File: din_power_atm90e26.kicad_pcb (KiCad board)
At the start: 2 copper layers, 86.9 x 32.8 mm, 60 parts, among them J1 CONN_01X06, J2 VBAT, J3 CONN_01X08, J4 CONN_02X18, J5 CONN_01X08, U1 MCP73831-2-OT, U2 TLV1117-33, U3 TLV1117-33, U4 Hi-Link_SMPS, U5 dc-dc

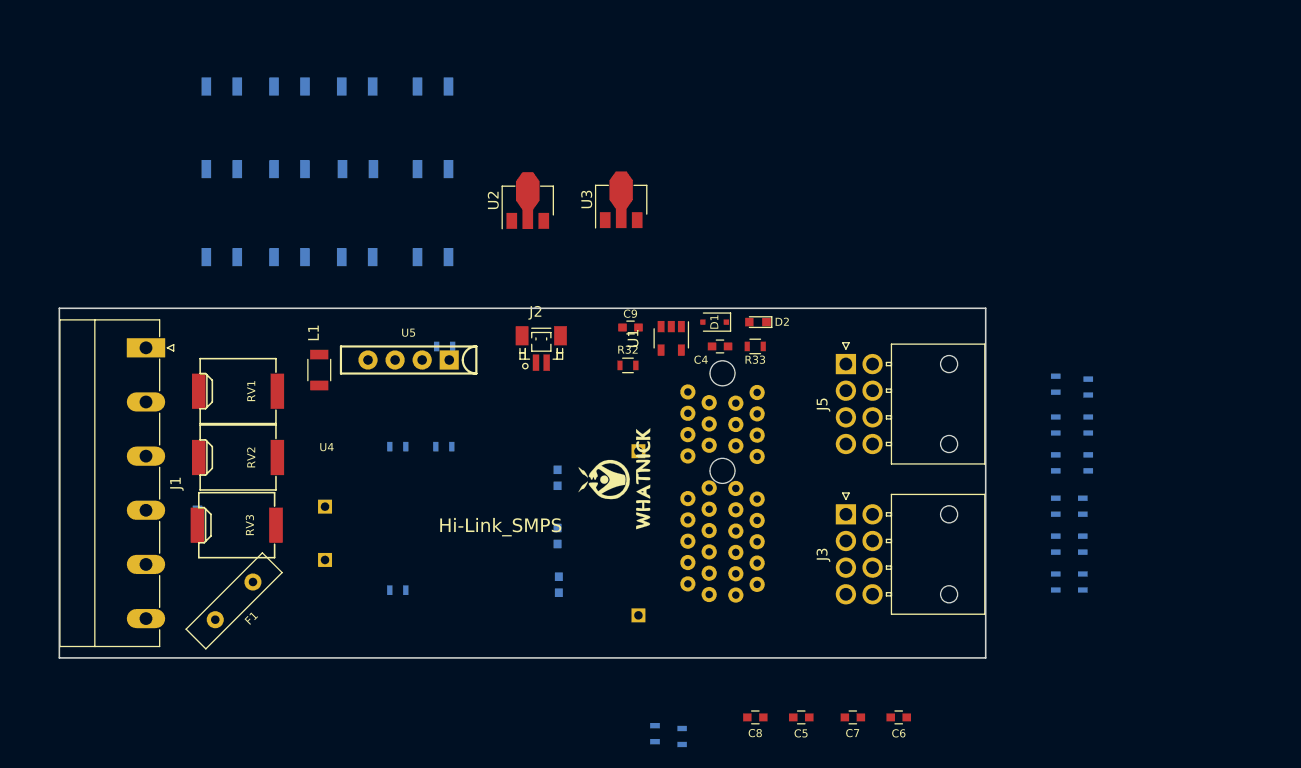
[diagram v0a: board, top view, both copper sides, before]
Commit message: Layout footprints
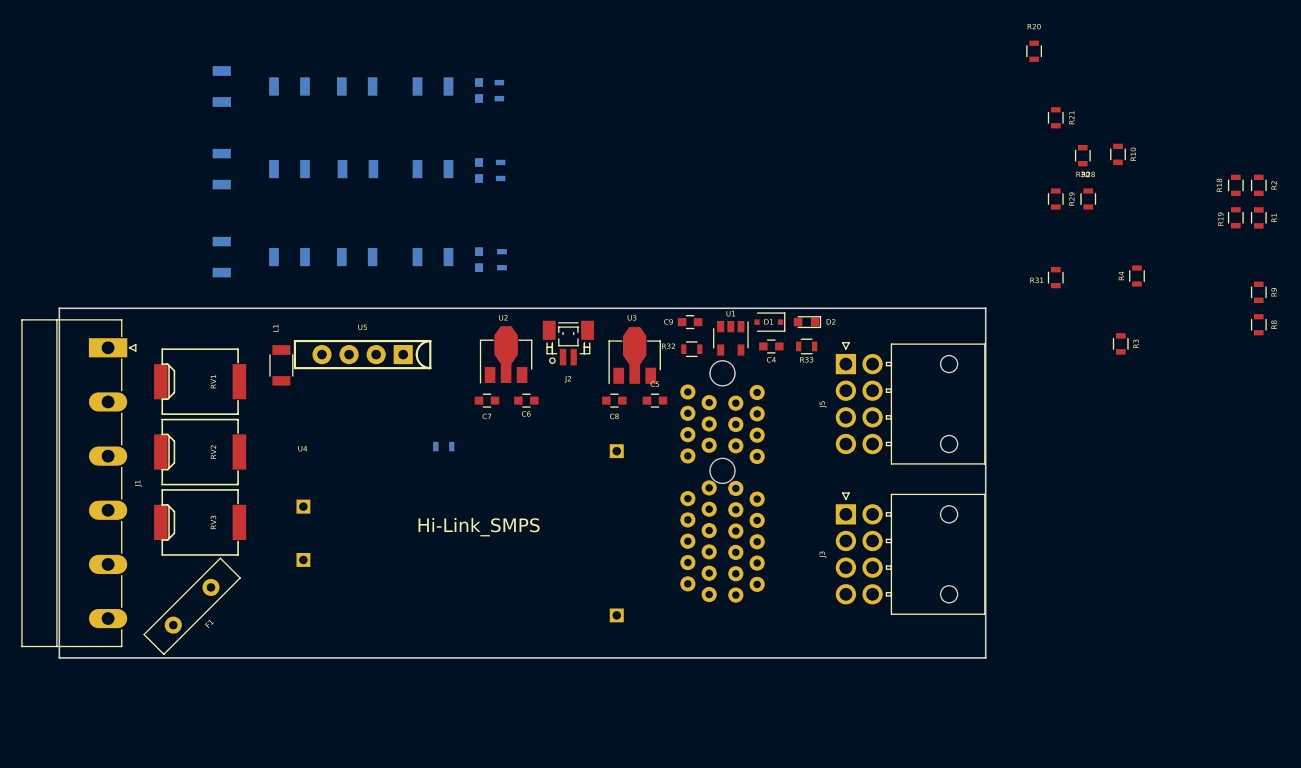
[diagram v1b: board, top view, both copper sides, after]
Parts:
- G1: moved to B.Cu
- R1, R10, R18, R19, R2, R20, R21, R28, R29, R3, R30, R31, R4, R8, R9: moved to F.Cu
- moved R3 88.1 mm to (205.5, 48.8), turned to 270 degrees
- moved R9 85.5 mm to (218.4, 44.0), turned to 270 degrees
- moved R8 81.6 mm to (218.4, 47.0), turned to 270 degrees
- moved R1 74.5 mm to (218.4, 37.0), turned to 270 degrees
- moved R10 65.7 mm to (205.2, 31.0), turned to 270 degrees
- moved R25 61.9 mm to (147.2, 25.0), turned to 90 degrees
- moved R4 60.7 mm to (207.0, 42.4), turned to 90 degrees
- moved R26 60.1 mm to (147.3, 32.5), turned to 90 degrees
- moved R27 54.2 mm to (147.4, 40.9), turned to 90 degrees
- moved R20 49.8 mm to (197.4, 21.3), turned to 90 degrees
- moved C6 45.9 mm to (149.7, 54.1), turned to 180 degrees
- moved C7 45.4 mm to (146.0, 54.1)
- moved R2 40.7 mm to (218.4, 33.9), turned to 270 degrees
- moved R21 40.0 mm to (199.4, 27.6), turned to 90 degrees
- moved C3 37.1 mm to (145.3, 25.0)
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
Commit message: Layout footprints
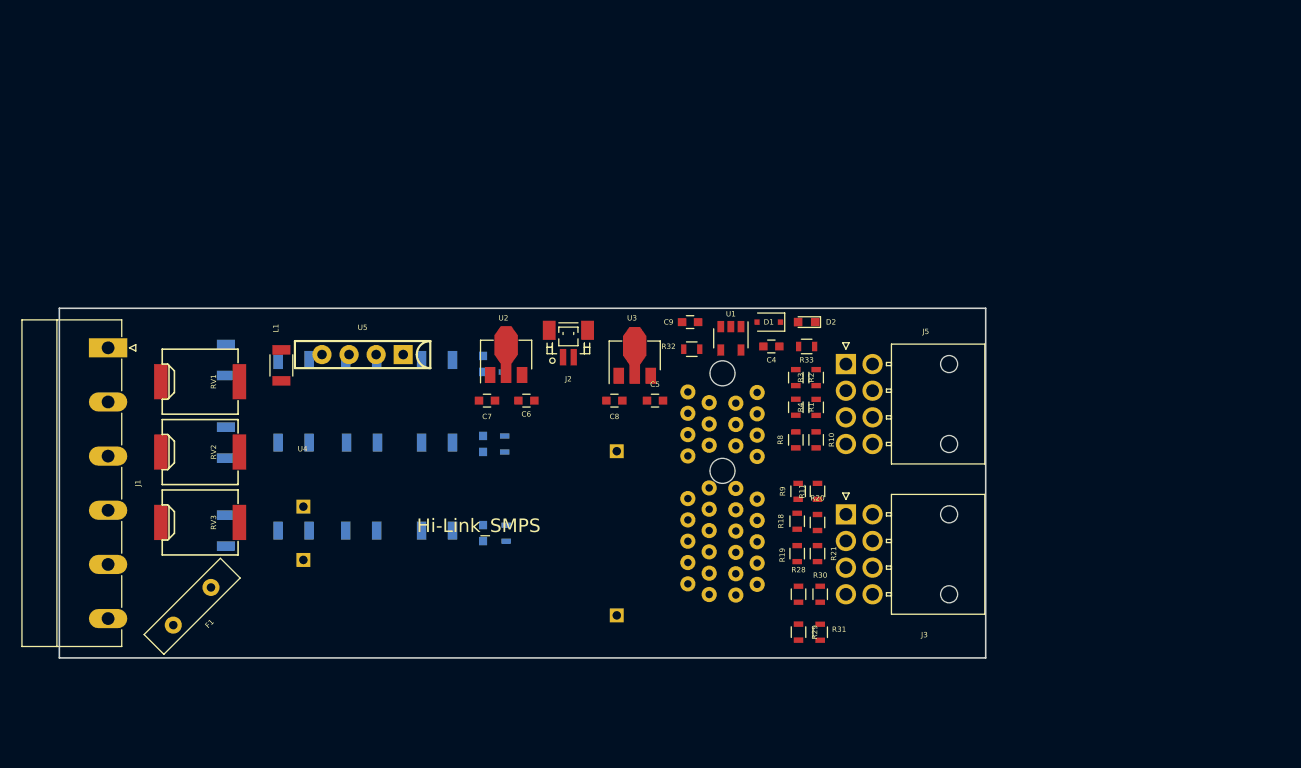
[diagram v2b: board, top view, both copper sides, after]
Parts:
- R11: moved to F.Cu
- moved R18 51.8 mm to (175.1, 65.4)
- moved R19 51.8 mm to (175.1, 68.5)
- moved R20 48.7 mm to (177.0, 65.6)
- moved R30 48.0 mm to (177.3, 72.3), turned to 90 degrees
- moved R29 47.3 mm to (175.3, 75.8)
- moved R9 47.1 mm to (175.2, 62.6), turned to 90 degrees
- moved R2 47.0 mm to (175.0, 52.0)
- moved R1 46.9 mm to (175.0, 54.8)
- moved R21 46.6 mm to (177.0, 68.5)
- moved R28 46.0 mm to (175.3, 72.3)
- moved R8 44.8 mm to (175.0, 57.8), turned to 90 degrees
- moved R31 39.9 mm to (177.3, 75.9), turned to 90 degrees
- moved R10 39.0 mm to (176.9, 57.8)
- moved R11 35.3 mm to (177.0, 62.6), turned to 90 degrees
- moved R4 32.5 mm to (176.9, 54.8)
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
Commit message: Changes from urbito
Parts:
- C1, C2, C3, R12, R13, R14, R15, R16, R17, R22, R23, R24, R25, R26, R27, R5, R6, R7: moved to F.Cu
- R10, R11, R20, R21, R3, R30, R31, R4, U4: moved to B.Cu
- moved R6 34.3 mm to (154.5, 67.6), turned to 90 degrees
- moved R13 31.2 mm to (154.5, 74.2), turned to 90 degrees
- moved F1 24.4 mm to (141.4, 59.7)
- moved R16 22.4 mm to (149.8, 74.2), turned to 270 degrees
- moved U5 21.9 mm to (152.0, 62.7)
- moved R26 17.6 mm to (142.4, 74.9), turned to 270 degrees
- moved C1 17.6 mm to (140.4, 75.0), turned to 90 degrees
- moved R23 16.6 mm to (145.2, 74.2), turned to 90 degrees
- moved U1 14.5 mm to (154.5, 49.9)
- moved C7 14.4 mm to (131.7, 53.6)
- moved D1 14.1 mm to (158.8, 49.9), turned to 90 degrees
- moved U2 13.9 mm to (133.9, 49.5)
- moved C6 13.8 mm to (135.9, 53.5)
- moved R33 13.4 mm to (162.8, 50.8)
- moved R27 12.7 mm to (138.3, 75.0), turned to 270 degrees
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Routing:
- net GNDA: track 0.00 -> 171.9 mm, vias 0 -> 7
- net GNDPWR: track 0.00 -> 89.6 mm, vias 0 -> 6
- net IB2+: track 0.00 -> 89.3 mm, vias 0 -> 2
- net IA1-: track 0.00 -> 87.3 mm, vias 0 -> 5
- net IB2-: track 0.00 -> 72.9 mm
- net +5V: track 0.00 -> 69.5 mm, vias 0 -> 3
- net IC1-: track 0.00 -> 64.7 mm, vias 0 -> 2
- net +3.3V_ISO: track 0.00 -> 57.1 mm, vias 0 -> 9
- net IB1-: track 0.00 -> 55.9 mm, vias 0 -> 1
- net IN2-: track 0.00 -> 53.6 mm
- net IC2-: track 0.00 -> 50.7 mm, vias 0 -> 1
- net UN: track 0.00 -> 50.4 mm, vias 0 -> 3
- net +3V3: track 0.00 -> 50.3 mm, vias 0 -> 2
- net IN2+: track 0.00 -> 49.5 mm, vias 0 -> 2
- net UB: track 0.00 -> 47.2 mm
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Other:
- rule trace_min: 0.2 -> 0.1
- rule via_min_drill: 0.3 -> 0.2
- rule via_min_size: 0.4 -> 0.3
